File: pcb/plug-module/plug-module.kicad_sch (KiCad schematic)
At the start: 15 parts, among them J1 Conn_01x10_Pin, J2 Conn_01x04_Pin, J3 Conn_01x15_Socket, J4 Conn_01x04_Pin, J5 Conn_01x10_Pin, Q1 BS170, U1 74HC688, U2 74AHC1G08, U3 74HC595

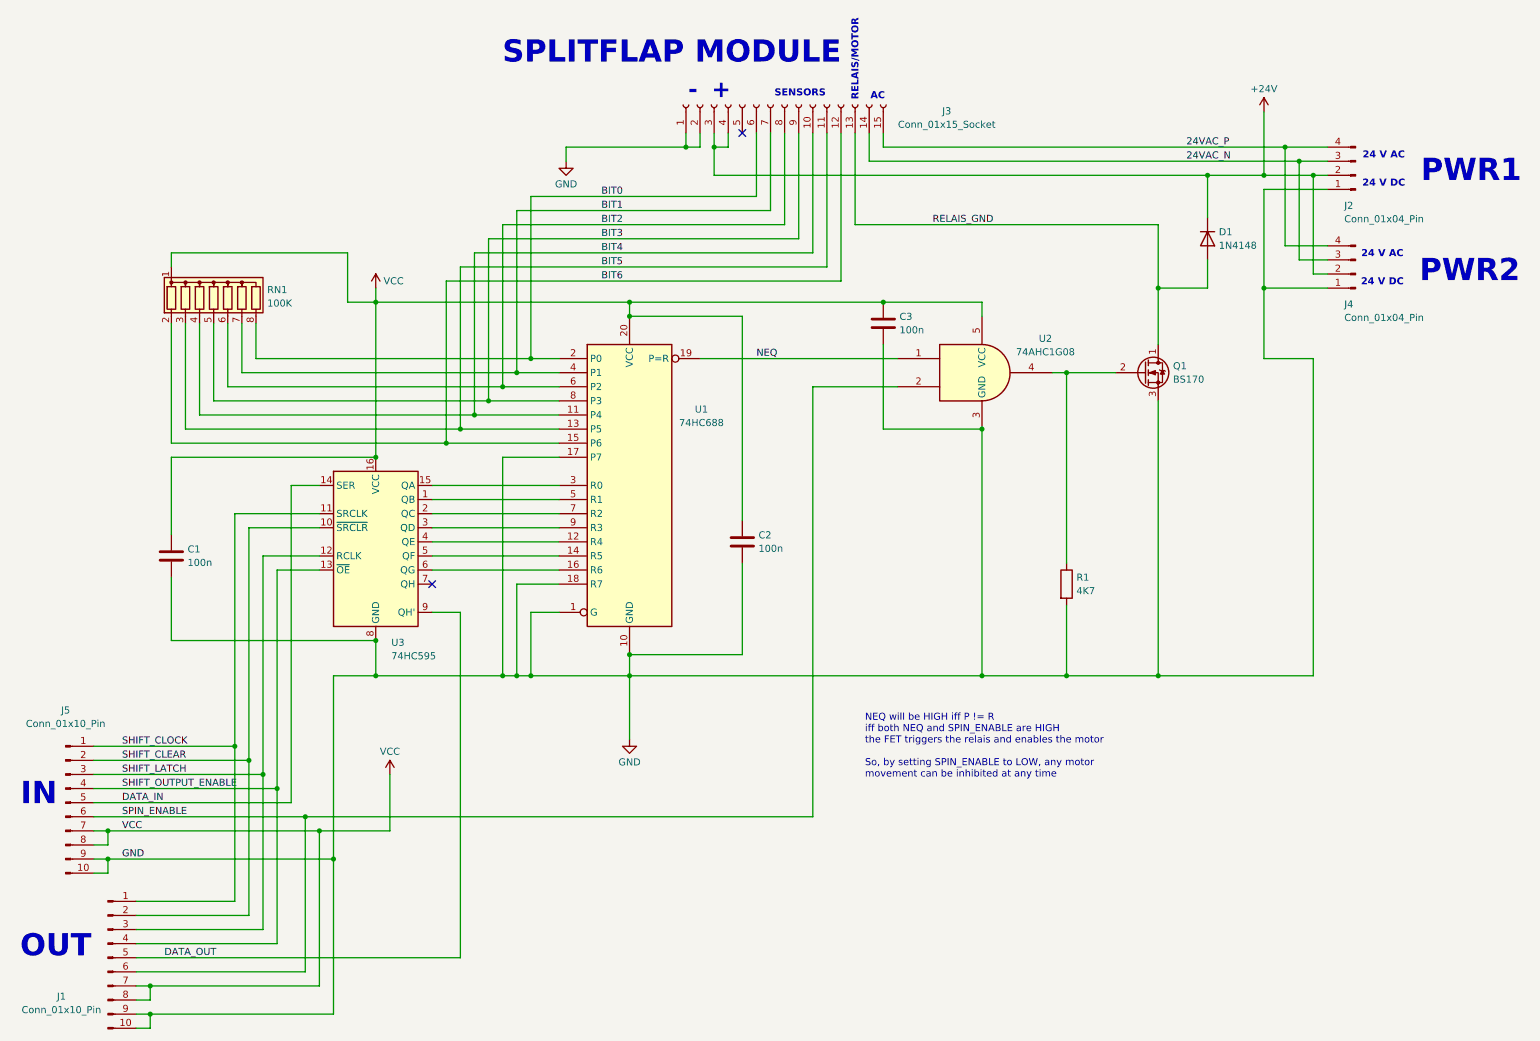
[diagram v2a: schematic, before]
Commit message: snubber, terminal resistors
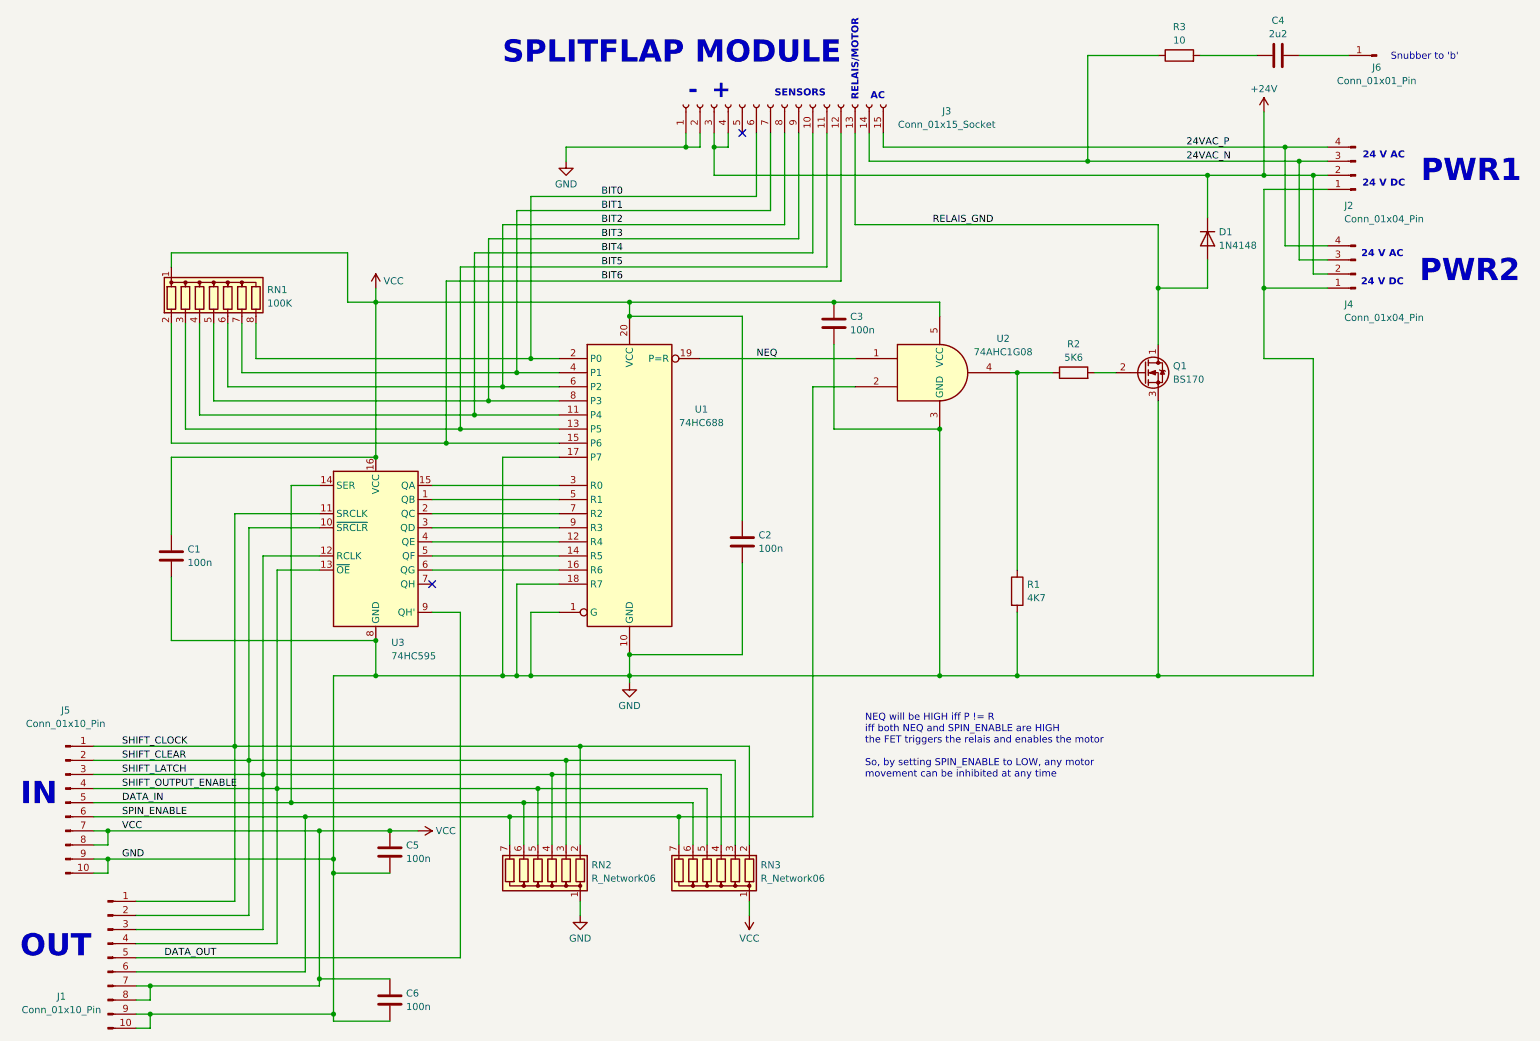
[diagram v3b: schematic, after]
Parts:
- added C4: 2u2, symbol Device:C
- added C5, C6: 100n, symbol Device:C
- added J6: Conn_01x01_Pin, symbol Connector:Conn_01x01_Pin
- added R2: 5K6, symbol Device:R
- added R3: 10, symbol Device:R
- added RN2, RN3: R_Network06, Resistor_THT:R_Array_SIP7, symbol Device:R_Network06
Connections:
- net 24VAC_N: now also R3.1
- net DATA_IN: now also RN2.6 (R5), RN3.6 (R5)
- net GND: now also C5.2, C6.2, RN2.1 (common)
- net SHIFT_CLEAR: now also RN2.3 (R2), RN3.3 (R2)
- net SHIFT_CLOCK: now also RN2.2 (R1), RN3.2 (R1)
- net SHIFT_LATCH: now also RN2.4 (R3), RN3.4 (R3)
- net SHIFT_OUTPUT_ENABLE: now also RN2.5 (R4), RN3.5 (R4)
- net SPIN_ENABLE: now also RN2.7 (R6), RN3.7 (R6)
- net VCC: now also C5.1, C6.1, RN3.1 (common)
- net at R1.1, U2.4: now also R2.1; no longer Q1.2 (G)
- new net: C4.2, J6.1 (Pin_1)
- new net: Q1.2 (G), R2.2
- new net: C4.1, R3.2
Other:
- note added: "Snubber to 'b'"
- moved on the sheet: C3, R1, U2

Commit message: pcb layout plug module
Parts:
- removed RN2, RN3: R_Network06, Resistor_THT:R_Array_SIP7, symbol Device:R_Network06
- added J7, J8: Conn_01x01_Pin, TestPoint:TestPoint_Pad_4.0x4.0mm, symbol Connector:Conn_01x01_Pin
- added RN2, RN3: R_Network05, Resistor_THT:R_Array_SIP6, symbol Device:R_Network05
- C4, C5, C6: footprint (none) -> Capacitor_THT:C_Disc_D4.3mm_W1.9mm_P5.00mm
- D1: footprint Diode_THT:D_T-1_P5.08mm_Horizontal -> Diode_THT:D_T-1_P10.16mm_Horizontal
- J6: footprint (none) -> Connector_PinHeader_2.54mm:PinHeader_1x01_P2.54mm_Horizontal
- R2, R3: footprint (none) -> Resistor_THT:R_Axial_DIN0207_L6.3mm_D2.5mm_P10.16mm_Horizontal
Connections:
- net GND: now also J7.1 (Pin_1), J8.1 (Pin_1), RN2.1 (common)
- net SHIFT_CLEAR: now also RN2.2 (R1), RN3.2 (R1)
- net SHIFT_CLOCK: now also RN2.3 (R2), RN3.3 (R2)
- net SHIFT_LATCH: now also RN2.5 (R4), RN3.5 (R4)
- net SHIFT_OUTPUT_ENABLE: now also RN2.4 (R3), RN3.4 (R3)
- net SPIN_ENABLE: now also RN2.6 (R5), RN3.6 (R5)
- net VCC: now also RN3.1 (common)

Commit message: many improvements
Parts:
- added J10, J9: Conn_01x01_Pin, JS_Local:Langloch-Pad, symbol Connector:Conn_01x01_Pin
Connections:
- net GND: now also J10.1 (Pin_1), J9.1 (Pin_1)
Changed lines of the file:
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@@
 	)
 	(junction
+		(at 259.08 113.03)
+		(diameter 0)
+		(color 0 0 0 0)
+	)
+	(junction
 		(at 193.04 77.47)
 		(diameter 0)
@@
 	(wire
 		(pts
+			(xy 259.08 132.08) (xy 259.08 113.03)
+		)
+		(stroke
+			(width 0)
+			(type default)
+		)
+	)
+	(wire
+		(pts
 			(xy 153.67 53.34) (xy 97.79 53.34)
 		)
@@
 	(wire
 		(pts
+			(xy 259.08 113.03) (xy 259.08 105.41)
+		)
+		(stroke
+			(width 0)
+			(type default)
+		)
+	)
+	(wire
+		(pts
 			(xy 161.29 34.29) (xy 161.29 60.96)
 		)
@@
 	(wire
 		(pts
+			(xy 259.08 105.41) (xy 269.24 105.41)
+		)
+		(stroke
+			(width 0)
+			(type default)
+		)
+	)
+	(wire
+		(pts
 			(xy 153.67 34.29) (xy 153.67 53.34)
 		)
@@
 	(wire
 		(pts
+			(xy 259.08 113.03) (xy 269.24 113.03)
+		)
+		(stroke
+			(width 0)
+			(type default)
+		)
+	)
+	(wire
+		(pts
 			(xy 237.49 74.93) (xy 246.38 74.93)
 		)
@@
 	)
 	(symbol
+		(lib_id "Connector:Conn_01x01_Pin")
+		(at 274.32 113.03 180)
+		(unit 1)
+		(exclude_from_sim no)
+		(in_bom yes)
+		(on_board yes)
+		(dnp no)
+		(fields_autoplaced yes)
+		(property "Reference" "J10"
+			(at 273.685 108.8093 0)
+			(effects
+				(font
+					(size 1.27 1.27)
+				)
+			)
+		)
+		(property "Value" "Conn_01x01_Pin"
+			(at 273.685 111.2336 0)
+			(effects
+				(font
+					(size 1.27 1.27)
+				)
+			)
+		)
+		(property "Footprint" "JS_Local:Langloch-Pad"
+			(at 274.32 113.03 0)
+			(effects
+				(font
+					(size 1.27 1.27)
+				)
+				(hide yes)
+			)
+		)
+		(property "Datasheet" "~"
+			(at 274.32 113.03 0)
+			(effects
+				(font
+					(size 1.27 1.27)
+				)
+				(hide yes)
+			)
+		)
+		(property "Description" "Generic connector, single row, 01x01, script generated"
+			(at 274.32 113.03 0)
+			(effects
+				(font
+					(size 1.27 1.27)
+				)
+				(hide yes)
+			)
+		)
+		(pin "1"
+		)
+		(instances
+			(project "plug-module"
+				(path "/7d33117e-4f7b-4167-8883-44198fec4073"
+					(reference "J10")
+					(unit 1)
+				)
+			)
+		)
+	)
+	(symbol
 		(lib_id "power:VCC")
 		(at 144.78 175.26 180)
@@
 					(unit 1)
 				)
+			)
+		)
+	)
+	(symbol
+		(lib_id "Connector:Conn_01x01_Pin")
+		(at 274.32 105.41 180)
+		(unit 1)
+		(exclude_from_sim no)
+		(in_bom yes)
+		(on_board yes)
+		(dnp no)
+		(fields_autoplaced yes)
+		(property "Reference" "J9"
+			(at 273.685 101.1893 0)
+			(effects
+				(font
+					(size 1.27 1.27)
+				)
+			)
+		)
+		(property "Value" "Conn_01x01_Pin"
+			(at 273.685 103.6136 0)
+			(effects
+				(font
+					(size 1.27 1.27)
+				)
+			)
+		)
+		(property "Footprint" "JS_Local:Langloch-Pad"
+			(at 274.32 105.41 0)
+			(effects
+				(font
+					(size 1.27 1.27)
+				)
+				(hide yes)
+			)
+		)
+		(property "Datasheet" "~"
+			(at 274.32 105.41 0)
+			(effects
+				(font
+					(size 1.27 1.27)
+				)
+				(hide yes)
+			)
+		)
+		(property "Description" "Generic connector, single row, 01x01, script generated"
+			(at 274.32 105.41 0)
+			(effects
+				(font
+					(size 1.27 1.27)
+				)
+				(hide yes)
+			)
+		)
+		(pin "1"
+		)
+		(instances
+			(project "plug-module"
+				(path "/7d33117e-4f7b-4167-8883-44198fec4073"
+					(reference "J9")
+					(unit 1)
+				)

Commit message: graytable, both pcbs
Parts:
- removed RN2, RN3: R_Network05, Resistor_THT:R_Array_SIP6, symbol Device:R_Network05
- added R10, R11, R12, R13, R4, R5, R6, R7, R8, R9: R, Resistor_SMD:R_1206_3216Metric_Pad1.30x1.75mm_HandSolder, symbol Device:R
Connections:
- net GND: now also R4.2, R5.2, R6.2, R7.2, R8.2
- net SHIFT_CLEAR: now also R10.1, R5.1
- net SHIFT_CLOCK: now also R4.1, R9.1
- net SHIFT_LATCH: now also R11.1, R6.1
- net SHIFT_OUTPUT_ENABLE: now also R12.1, R7.1
- net SPIN_ENABLE: now also R13.1, R8.1
- net VCC: now also R10.2, R11.2, R12.2, R13.2, R9.2

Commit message: plug module pp snubber
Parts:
- added J11, J12: Conn_01x01_Pin, TestPoint:TestPoint_Pad_4.0x4.0mm, symbol Connector:Conn_01x01_Pin
- C4: footprint Capacitor_THT:C_Disc_D4.3mm_W1.9mm_P5.00mm -> Capacitor_THT:C_Rect_L18.0mm_W7.0mm_P15.00mm_FKS3_FKP3
- D1: value 1N4148 -> 1N4148/1N4003
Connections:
- net GND: now also J11.1 (Pin_1), J12.1 (Pin_1)
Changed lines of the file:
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@@
 	)
 	(junction
+		(at 259.08 139.7)
+		(diameter 0)
+		(color 0 0 0 0)
+	)
+	(junction
 		(at 161.29 172.72)
 		(diameter 0)
@@
 	)
 	(junction
+		(at 259.08 147.32)
+		(diameter 0)
+		(color 0 0 0 0)
+	)
+	(junction
 		(at 69.85 167.64)
 		(diameter 0)
@@
 	(wire
 		(pts
+			(xy 259.08 147.32) (xy 259.08 153.67)
+		)
+		(stroke
+			(width 0)
+			(type default)
+		)
+	)
+	(wire
+		(pts
 			(xy 179.07 87.63) (xy 179.07 132.08)
 		)
@@
 	(wire
 		(pts
+			(xy 259.08 153.67) (xy 269.24 153.67)
+		)
+		(stroke
+			(width 0)
+			(type default)
+		)
+	)
+	(wire
+		(pts
 			(xy 87.63 107.95) (xy 110.49 107.95)
 		)
@@
 	(wire
 		(pts
+			(xy 259.08 139.7) (xy 259.08 147.32)
+		)
+		(stroke
+			(width 0)
+			(type default)
+		)
+	)
+	(wire
+		(pts
 			(xy 161.29 172.72) (xy 161.29 175.26)
 		)
@@
 	(wire
 		(pts
+			(xy 259.08 147.32) (xy 269.24 147.32)
+		)
+		(stroke
+			(width 0)
+			(type default)
+		)
+	)
+	(wire
+		(pts
 			(xy 36.83 187.96) (xy 36.83 190.5)
 		)
@@
 	)
 	(symbol
+		(lib_id "Connector:Conn_01x01_Pin")
+		(at 274.32 153.67 180)
+		(unit 1)
+		(exclude_from_sim no)
+		(in_bom yes)
+		(on_board yes)
+		(dnp no)
+		(fields_autoplaced yes)
+		(property "Reference" "J12"
+			(at 273.685 149.4493 0)
+			(effects
+				(font
+					(size 1.27 1.27)
+				)
+			)
+		)
+		(property "Value" "Conn_01x01_Pin"
+			(at 273.685 151.8736 0)
+			(effects
+				(font
+					(size 1.27 1.27)
+				)
+			)
+		)
+		(property "Footprint" "TestPoint:TestPoint_Pad_4.0x4.0mm"
+			(at 274.32 153.67 0)
+			(effects
+				(font
+					(size 1.27 1.27)
+				)
+				(hide yes)
+			)
+		)
+		(property "Datasheet" "~"
+			(at 274.32 153.67 0)
+			(effects
+				(font
+					(size 1.27 1.27)
+				)
+				(hide yes)
+			)
+		)
+		(property "Description" "Generic connector, single row, 01x01, script generated"
+			(at 274.32 153.67 0)
+			(effects
+				(font
+					(size 1.27 1.27)
+				)
+				(hide yes)
+			)
+		)
+		(pin "1"
+		)
+		(instances
+			(project "plug-module"
+				(path "/7d33117e-4f7b-4167-8883-44198fec4073"
+					(reference "J12")
+					(unit 1)
+				)
+			)
+		)
+	)
+	(symbol
 		(lib_id "Device:C")
 		(at 80.01 163.83 0)
@@
 			)
 		)
-		(property "Footprint" "Capacitor_THT:C_Disc_D4.3mm_W1.9mm_P5.00mm"
+		(property "Footprint" "Capacitor_THT:C_Rect_L18.0mm_W7.0mm_P15.00mm_FKS3_FKP3"
 			(at 243.84 19.3548 0)
 			(effects
@@
 		(on_board yes)
 		(dnp no)
-		(fields_autoplaced yes)
 		(property "Reference" "D1"
 			(at 229.362 52.1278 90)
@@
 			)
 		)
-		(property "Value" "1N4148"
-			(at 229.362 54.5521 90)
+		(property "Value" "1N4148/1N4003"
+			(at 224.536 61.468 0)
 			(effects
 				(font
 					(size 1.27 1.27)
 				)
-				(justify left)
+				(justify right)
 			)
 		)
@@
 					(unit 1)
 				)
+			)
+		)
+	)
+	(symbol
+		(lib_id "Connector:Conn_01x01_Pin")
+		(at 274.32 147.32 180)
+		(unit 1)
+		(exclude_from_sim no)
+		(in_bom yes)
+		(on_board yes)
+		(dnp no)
+		(fields_autoplaced yes)
+		(property "Reference" "J11"
+			(at 273.685 143.0993 0)
+			(effects
+				(font
+					(size 1.27 1.27)
+				)
+			)
+		)
+		(property "Value" "Conn_01x01_Pin"
+			(at 273.685 145.5236 0)
+			(effects
+				(font
+					(size 1.27 1.27)
+				)
+			)
+		)
+		(property "Footprint" "TestPoint:TestPoint_Pad_4.0x4.0mm"
+			(at 274.32 147.32 0)
+			(effects
+				(font
+					(size 1.27 1.27)
+				)
+				(hide yes)
+			)
+		)
+		(property "Datasheet" "~"
+			(at 274.32 147.32 0)
+			(effects
+				(font
+					(size 1.27 1.27)
+				)
+				(hide yes)
+			)
+		)
+		(property "Description" "Generic connector, single row, 01x01, script generated"
+			(at 274.32 147.32 0)
+			(effects
+				(font
+					(size 1.27 1.27)
+				)
+				(hide yes)
+			)
+		)
+		(pin "1"
+		)
+		(instances
+			(project "plug-module"
+				(path "/7d33117e-4f7b-4167-8883-44198fec4073"
+					(reference "J11")
+					(unit 1)
+				)

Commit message: review
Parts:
- RN1: value 100K -> 390K
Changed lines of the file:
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@@
 			)
 		)
-		(property "Value" "100K"
+		(property "Value" "390K"
 			(at 57.912 64.9661 0)
 			(effects
